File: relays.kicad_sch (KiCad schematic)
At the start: 15 parts, among them J301 relays, J302 relays, K301 G5V-1, K302 G5V-1, K303 G5V-1, K304 G5V-1, K305 G5V-1, K306 G5V-1, K307 G5V-1, K308 G5V-1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

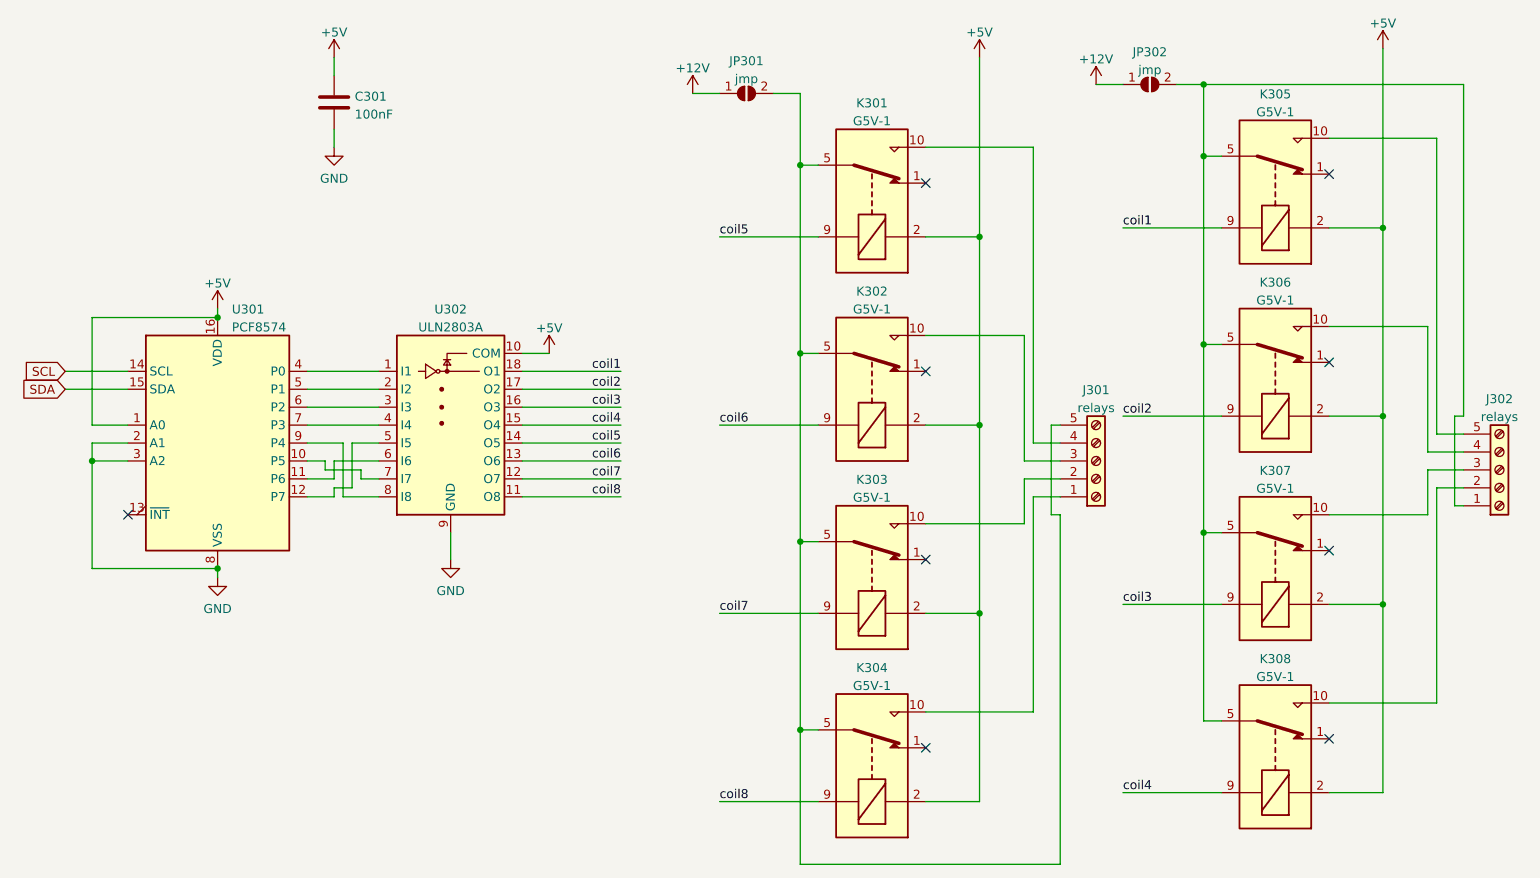
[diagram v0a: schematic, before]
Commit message: added something to debug the channel buttons
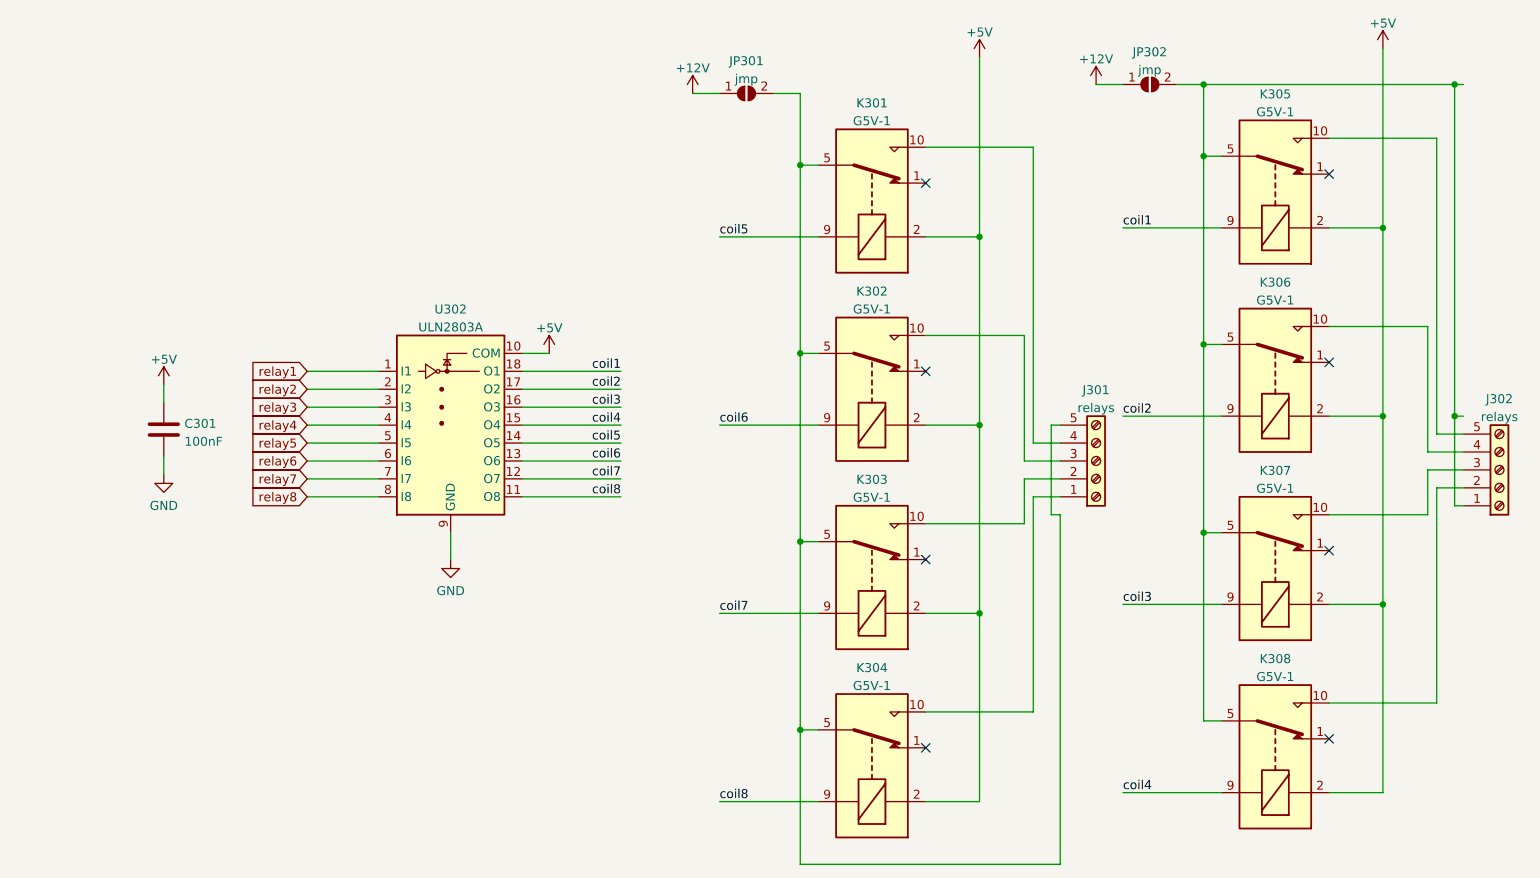
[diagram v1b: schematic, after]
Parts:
- removed U301: PCF8574, Package_DIP:DIP-16_W7.62mm_Socket, symbol Interface_Expansion:PCF8574
- C301: footprint Capacitor_THT:C_Disc_D3.0mm_W1.6mm_P2.50mm -> Capacitor_SMD:C_0805_2012Metric
- U302: footprint Package_DIP:DIP-18_W7.62mm_Socket -> Package_SO:SOIC-18W_7.5x11.6mm_P1.27mm
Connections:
- net relay7: now reaches U302.7 (I7)
- net relay6: now reaches U302.6 (I6)
- net relay5: now reaches U302.5 (I5)
- net relay1: now reaches U302.1 (I1)
- net relay2: now reaches U302.2 (I2)
- net relay3: now reaches U302.3 (I3)
- net relay4: now reaches U302.4 (I4)
- net relay8: now reaches U302.8 (I8)
- no-connect marks 9 -> 8
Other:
- moved on the sheet: C301
